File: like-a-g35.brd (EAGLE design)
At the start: 68.6 x 53.3 mm, 12 parts, among them U1 ARDUINOR3-DIMENSION, U2 FCI_8193_MICRO_USB, X1 G1, X2 G2, X3 G3, X4 POWER, X5 POWER, X6 POWER, X7 WS1, X8 WS2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

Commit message: Moved some labels around.
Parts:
- moved X4 1.27 mm to (34.3, 33.0)
- moved X5 1.27 mm to (34.3, 12.7)
- moved X7 1.27 mm to (34.3, 43.2)
- moved X8 1.27 mm to (34.3, 22.9)
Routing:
- net GDATA1: track 82.7 -> 47.9 mm, vias 0 -> 1
- net DATA2: track 54.0 -> 67.5 mm
- net +5V: track 142.3 -> 153.9 mm
- net GDATA3: track 33.0 -> 39.1 mm
- net CLK1: track 27.4 -> 26.1 mm, vias 1 -> 0
- net CLK2: track 44.1 -> 43.5 mm
- net DATA1: track 27.5 -> 27.3 mm, vias 1 -> 0
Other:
- board text added: "5V"
- board text added: "Blu GND"
- board text added: "Clk"
- board text added: "Data"
- board text added: "GND"
- board text added: "Red 5V"
- board text removed: "+ D -"
- board text removed: "Blue -"
- board text removed: "Red +"

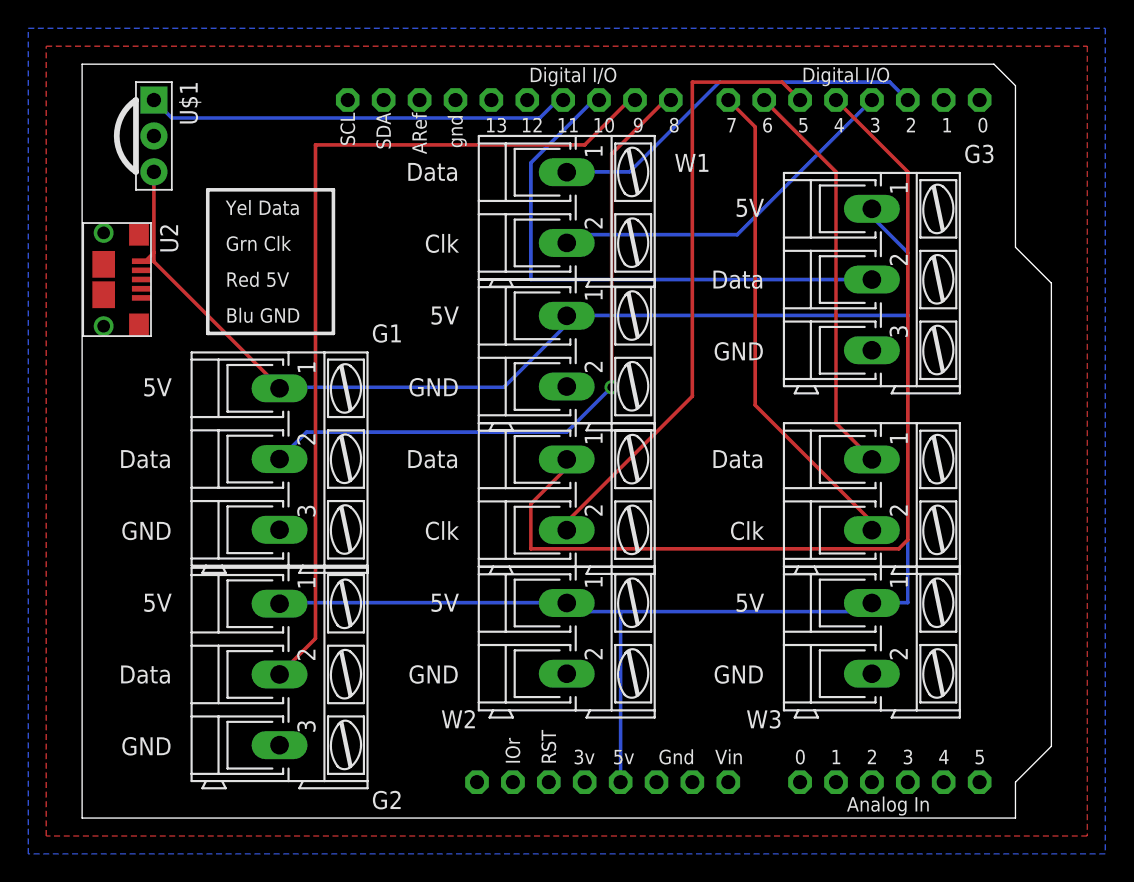
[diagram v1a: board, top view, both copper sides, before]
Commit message: Minor adjustments after previewing at OSH Park.
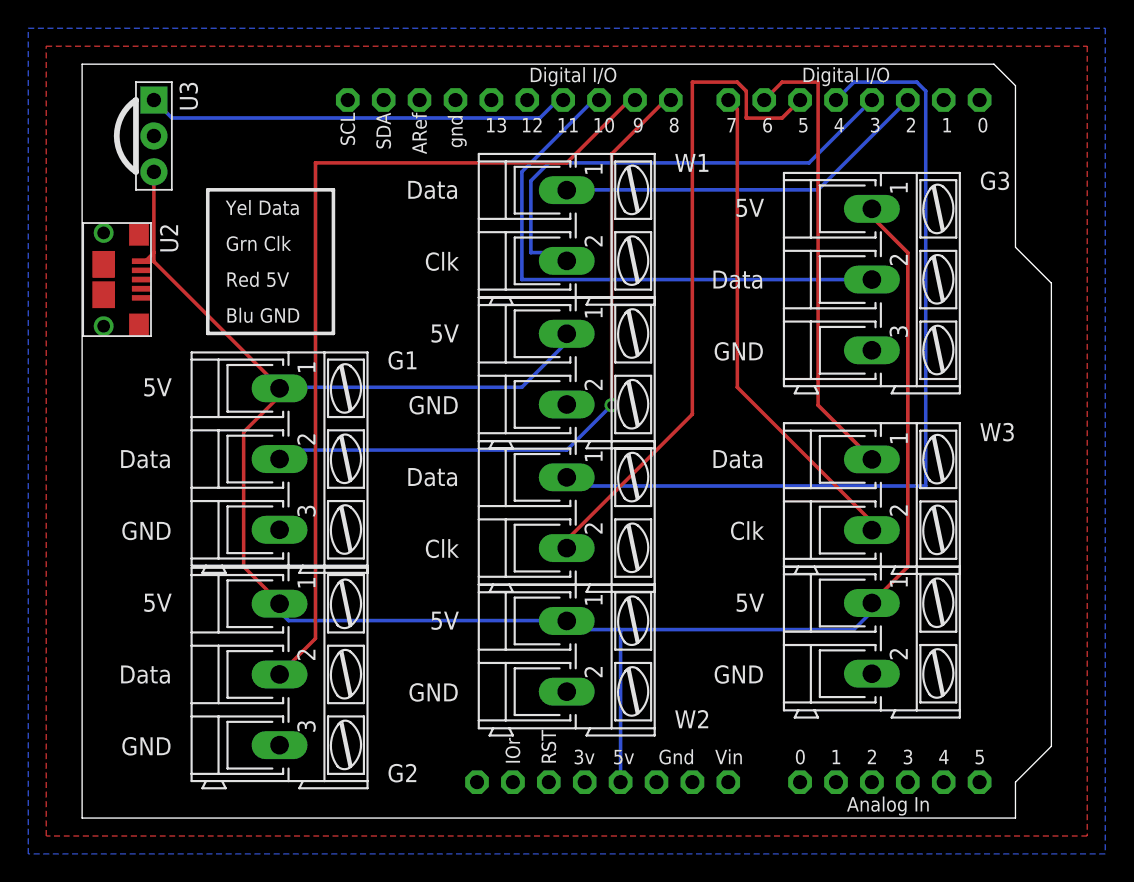
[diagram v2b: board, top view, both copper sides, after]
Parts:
- moved X4 1.27 mm to (34.3, 31.8)
- moved X7 1.27 mm to (34.3, 41.9)
- moved X5 1.27 mm to (34.3, 11.4)
- moved X8 1.27 mm to (34.3, 21.6)
- renumbered U$1 to U3
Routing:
- net +5V: track 153.9 -> 145.1 mm
- net CLK1: track 26.1 -> 34.7 mm
- net DATA2: track 67.5 -> 61.1 mm
- net DATA3: track 28.6 -> 32.6 mm
- net CLK2: track 43.5 -> 47.0 mm
- net GDATA3: track 39.1 -> 40.0 mm
- net GDATA1: track 47.9 -> 48.6 mm
- net GDATA2: track 62.4 -> 61.7 mm
- net DATA1: track 27.3 -> 26.8 mm
